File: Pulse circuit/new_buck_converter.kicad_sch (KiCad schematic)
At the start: 1 part, among them U5 MP1584EN(SOIC8E)

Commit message: little changes o the new buck converter
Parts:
- added C1: C, symbol Device:C
- added D1: D, symbol Device:D
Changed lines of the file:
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@@
 		(dnp no)
 		(fields_autoplaced yes)
-		(property "Reference" "U5"
+		(property "Reference" "U?"
 			(at 137.16 80.01 0)
 			(effects
@@
 				)
 			)
-		)
-	)
+			(project "new_buck_converter"
+				(path "/79a8c3b6-6b09-4ad6-9d05-49aaca02b087"
+					(reference "U?")
+					(unit 1)
+				)
+			)
+		)
+	)
+	(symbol
+		(lib_id "Device:D")
+		(at 166.37 68.58 0)
+		(unit 1)
+		(exclude_from_sim no)
+		(in_bom yes)
+		(on_board yes)
+		(dnp no)
+		(fields_autoplaced yes)
+		(property "Reference" "D1"
+			(at 166.37 62.23 0)
+			(effects
+				(font
+					(size 1.27 1.27)
+				)
+			)
+		)
+		(property "Value" "D"
+			(at 166.37 64.77 0)
+			(effects
+				(font
+					(size 1.27 1.27)
+				)
+			)
+		)
+		(property "Footprint" ""
+			(at 166.37 68.58 0)
+			(effects
+				(font
+					(size 1.27 1.27)
+				)
+				(hide yes)
+			)
+		)
+		(property "Datasheet" "~"
+			(at 166.37 68.58 0)
+			(effects
+				(font
+					(size 1.27 1.27)
+				)
+				(hide yes)
+			)
+		)
+		(property "Description" "Diode"
+			(at 166.37 68.58 0)
+			(effects
+				(font
+					(size 1.27 1.27)
+				)
+				(hide yes)
+			)
+		)
+		(property "Sim.Device" "D"
+			(at 166.37 68.58 0)
+			(effects
+				(font
+					(size 1.27 1.27)
+				)
+				(hide yes)
+			)
+		)
+		(property "Sim.Pins" "1=K 2=A"
+			(at 166.37 68.58 0)
+			(effects
+				(font
+					(size 1.27 1.27)
+				)
+				(hide yes)
+			)
+		)
+		(pin "1"
+		)
+		(pin "2"
+		)
+		(instances
+			(project ""
+				(path "/79a8c3b6-6b09-4ad6-9d05-49aaca02b087"
+					(reference "D1")
+					(unit 1)
+				)
+			)
+		)
+	)
+	(symbol
+		(lib_id "Device:C")
+		(at 175.26 82.55 0)
+		(unit 1)
+		(exclude_from_sim no)
+		(in_bom yes)
+		(on_board yes)
+		(dnp no)
+		(fields_autoplaced yes)
+		(property "Reference" "C1"
+			(at 179.07 81.2799 0)
+			(effects
+				(font
+					(size 1.27 1.27)
+				)
+				(justify left)
+			)
+		)
+		(property "Value" "C"
+			(at 179.07 83.8199 0)
+			(effects
+				(font
+					(size 1.27 1.27)
+				)
+				(justify left)
+			)
+		)
+		(property "Footprint" ""
+			(at 176.2252 86.36 0)
+			(effects
+				(font
+					(size 1.27 1.27)
+				)
+				(hide yes)
+			)
+		)
+		(property "Datasheet" "~"
+			(at 175.26 82.55 0)
+			(effects
+				(font
+					(size 1.27 1.27)
+				)
+				(hide yes)
+			)
+		)
+		(property "Description" "Unpolarized capacitor"
+			(at 175.26 82.55 0)
+			(effects
+				(font
+					(size 1.27 1.27)
+				)
+				(hide yes)
+			)
+		)
+		(pin "1"
+		)
+		(pin "2"
+		)
+		(instances
+			(project ""
+				(path "/79a8c3b6-6b09-4ad6-9d05-49aaca02b087"
+					(reference "C1")
+					(unit 1)
+				)
+			)
+		)
+	)
+	(sheet_instances
+		(path "/"
+			(page "1")
+		)
+	)
+	(embedded_fonts no)
 )

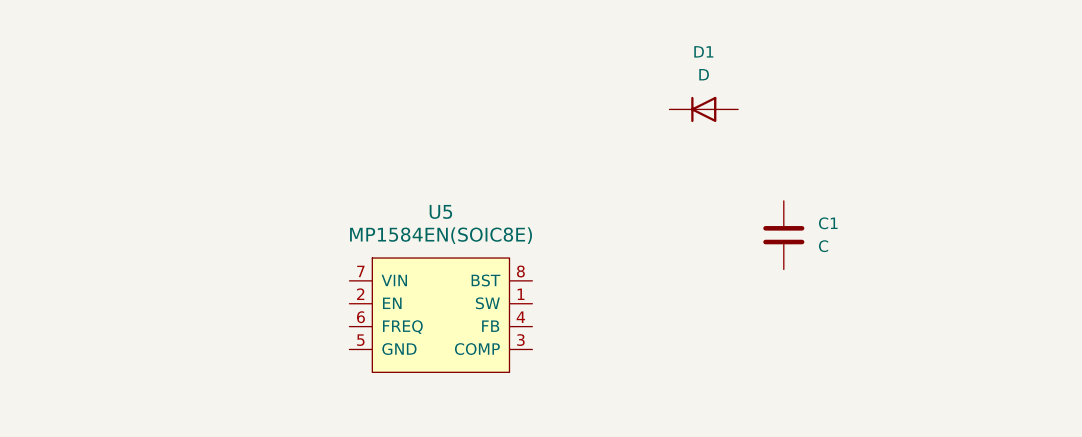
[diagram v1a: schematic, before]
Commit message: edited the new buck converter design
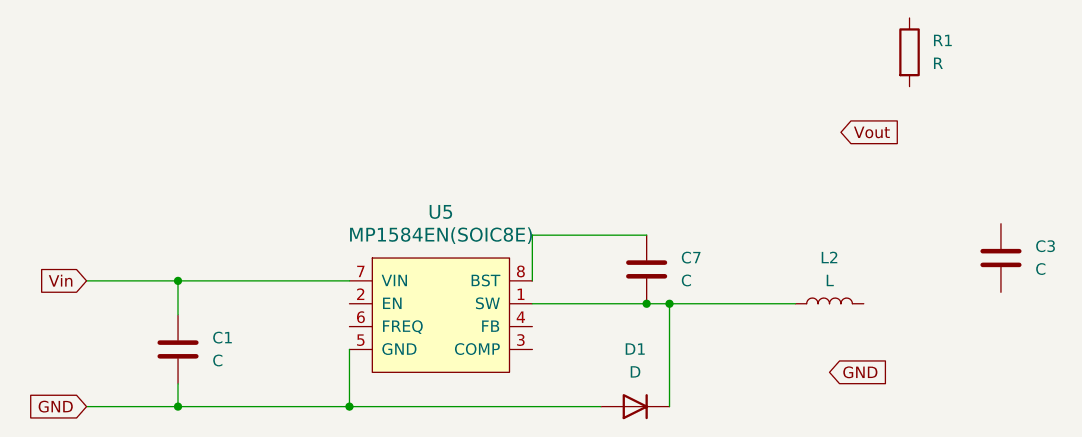
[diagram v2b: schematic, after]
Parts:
- added C3, C7: C, symbol Device:C
- added L2: L, symbol Device:L
- added R1: R, symbol Device:R
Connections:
- net at U5.1 (SW): now also D1.1 (K), C7.2, L2.1
- net GND: now reaches U5.5 (GND), U5.EP, U5.EP1 (EP@1)
- net GND: now also C1.2, D1.2 (A)
- net Vin: now reaches U5.7 (VIN)
- net Vin: now also C1.1
- net at U5.8 (BST): now also C7.1
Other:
- moved on the sheet: C1, D1

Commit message: Changed the annotations
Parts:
- renumbered C1 to C7, C7 to C8, C3 to C9, D1 to D2
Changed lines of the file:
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@@
 		(dnp no)
 		(fields_autoplaced yes)
-		(property "Reference" "D1"
+		(property "Reference" "D2"
 			(at 158.75 95.25 0)
 			(effects
@@
 			(project "Pulse circuit"
 				(path "/59caed24-c499-43df-90b9-3ac3a8609322/0afa37a8-64ca-4e6b-9013-61cb70edd3e2"
-					(reference "D1")
+					(reference "D2")
 					(unit 1)
 				)
@@
 		(dnp no)
 		(fields_autoplaced yes)
-		(property "Reference" "C3"
+		(property "Reference" "C9"
 			(at 203.2 83.8199 0)
 			(effects
@@
 			(project ""
 				(path "/59caed24-c499-43df-90b9-3ac3a8609322/0afa37a8-64ca-4e6b-9013-61cb70edd3e2"
-					(reference "C3")
+					(reference "C9")
 					(unit 1)
 				)
@@
 		(dnp no)
 		(fields_autoplaced yes)
-		(property "Reference" "C1"
+		(property "Reference" "C7"
 			(at 111.76 93.9799 0)
 			(effects
@@
 			(project "Pulse circuit"
 				(path "/59caed24-c499-43df-90b9-3ac3a8609322/0afa37a8-64ca-4e6b-9013-61cb70edd3e2"
-					(reference "C1")
+					(reference "C7")
 					(unit 1)
 				)
@@
 		(dnp no)
 		(fields_autoplaced yes)
-		(property "Reference" "C7"
+		(property "Reference" "C8"
 			(at 163.83 85.0899 0)
 			(effects
@@
 			(project ""
 				(path "/59caed24-c499-43df-90b9-3ac3a8609322/0afa37a8-64ca-4e6b-9013-61cb70edd3e2"
-					(reference "C7")
-					(unit 1)
-				)
+					(reference "C8")
+					(unit 1)
+				)

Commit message: values added to buck converter
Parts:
- renumbered C7 to C1, C9 to C3, C8 to C7, D2 to D1
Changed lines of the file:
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@@
 		(dnp no)
 		(fields_autoplaced yes)
-		(property "Reference" "D2"
+		(property "Reference" "D1"
 			(at 158.75 95.25 0)
 			(effects
@@
 			(project "Pulse circuit"
 				(path "/59caed24-c499-43df-90b9-3ac3a8609322/0afa37a8-64ca-4e6b-9013-61cb70edd3e2"
-					(reference "D2")
+					(reference "D1")
 					(unit 1)
 				)
@@
 		(dnp no)
 		(fields_autoplaced yes)
-		(property "Reference" "C9"
+		(property "Reference" "C3"
 			(at 203.2 83.8199 0)
 			(effects
@@
 			(project ""
 				(path "/59caed24-c499-43df-90b9-3ac3a8609322/0afa37a8-64ca-4e6b-9013-61cb70edd3e2"
-					(reference "C9")
+					(reference "C3")
 					(unit 1)
 				)
@@
 		(dnp no)
 		(fields_autoplaced yes)
-		(property "Reference" "C7"
+		(property "Reference" "C1"
 			(at 111.76 93.9799 0)
 			(effects
@@
 			(project "Pulse circuit"
 				(path "/59caed24-c499-43df-90b9-3ac3a8609322/0afa37a8-64ca-4e6b-9013-61cb70edd3e2"
-					(reference "C7")
+					(reference "C1")
 					(unit 1)
 				)
@@
 		(dnp no)
 		(fields_autoplaced yes)
-		(property "Reference" "C8"
+		(property "Reference" "C7"
 			(at 163.83 85.0899 0)
 			(effects
@@
 			(project ""
 				(path "/59caed24-c499-43df-90b9-3ac3a8609322/0afa37a8-64ca-4e6b-9013-61cb70edd3e2"
-					(reference "C8")
-					(unit 1)
-				)
+					(reference "C7")
+					(unit 1)
+				)
